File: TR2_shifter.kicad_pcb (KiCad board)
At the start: 2 copper layers, 69.2 x 29.8 mm, 28 parts, among them U1 LM339_DIP, U2 LM339_DIP

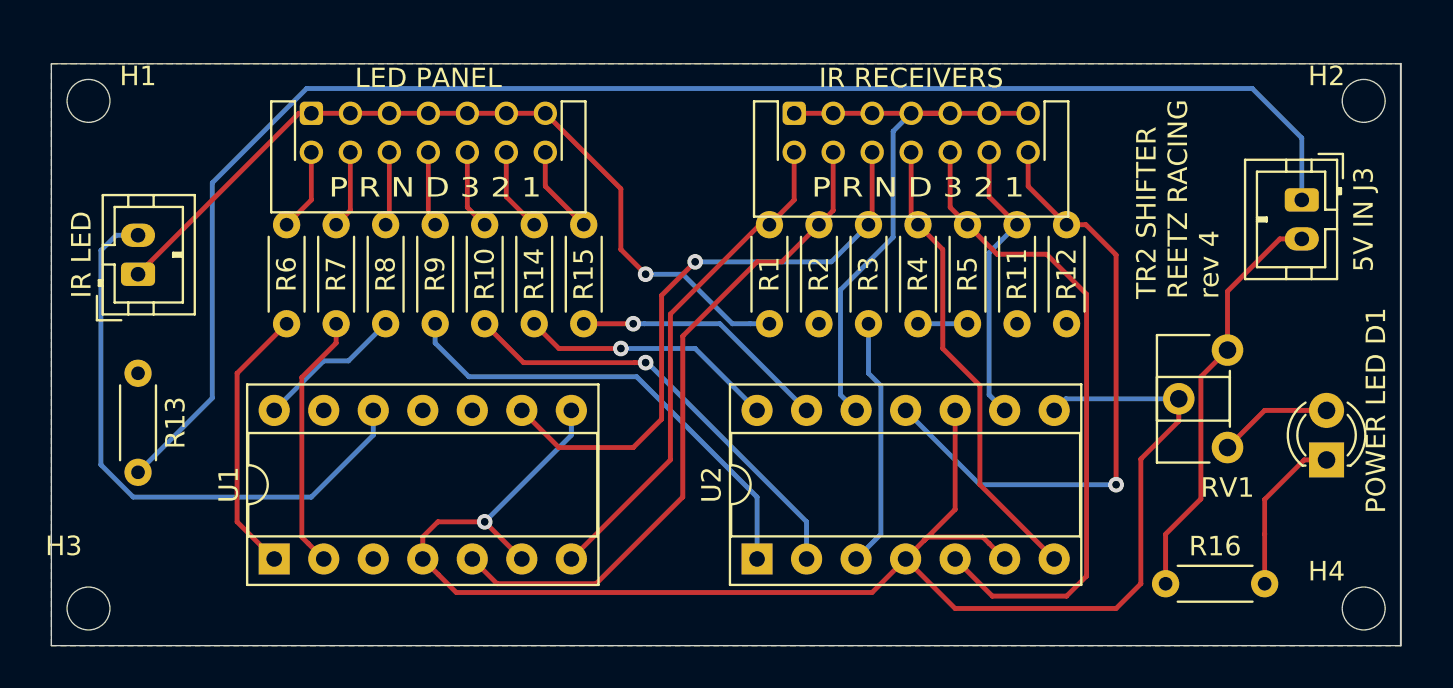
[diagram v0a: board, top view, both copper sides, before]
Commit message: Update silk and shift a few components
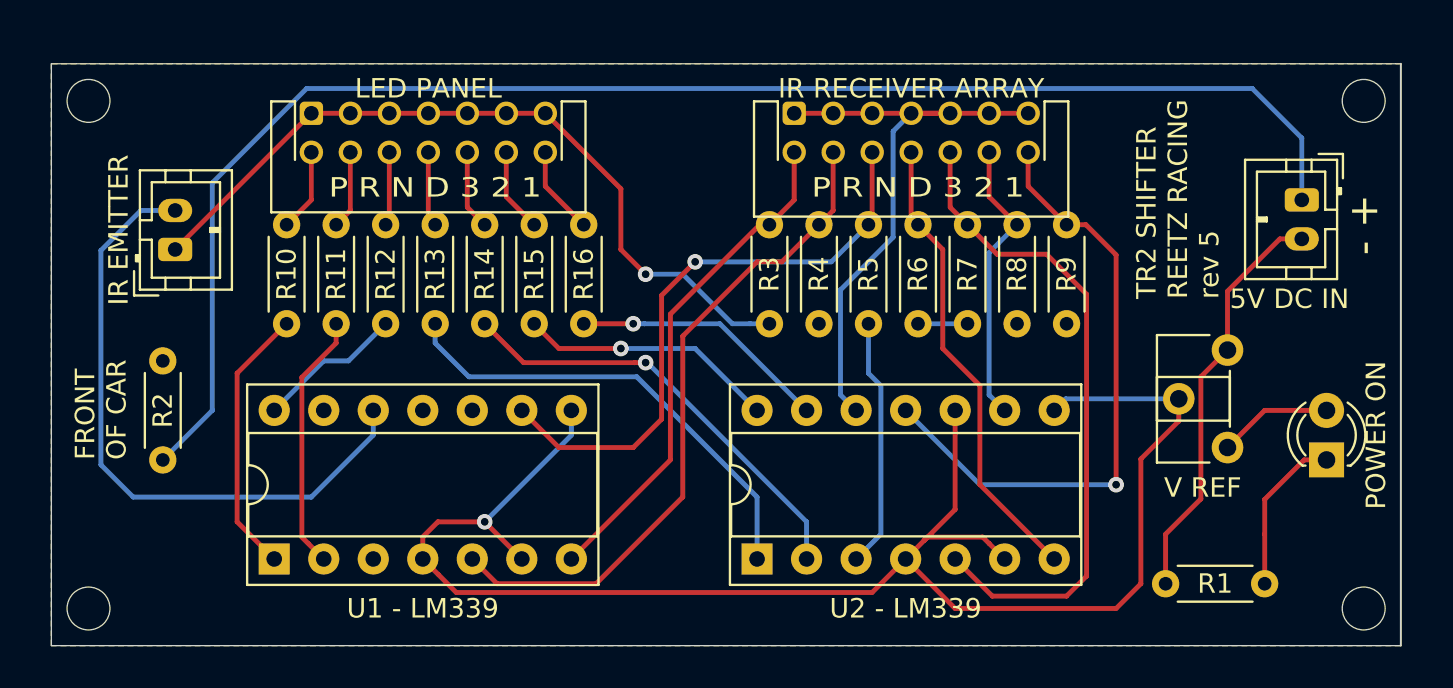
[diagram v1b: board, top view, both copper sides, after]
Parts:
- 5V DC IN: renamed from 5V IN J3
- IR EMITTER: renamed from IR LED
- IR RECEIVER ARRAY: renamed from IR RECEIVERS
- POWER ON: renamed from POWER LED D1
- U1 - LM339: renamed from U1
- U2 - LM339: renamed from U2
- V REF: renamed from RV1
- moved IR EMITTER 2.29 mm to (158.1, 78.1)
- moved R2 1.42 mm to (157.5, 83.8)
- renumbered R16 to R1, R6 to R10, R7 to R11, R8 to R12, R9 to R13, R10 to R14, R14 to R15, R15 to R16, R13 to R2, R1 to R3, R2 to R4, R3 to R5, R4 to R6, R5 to R7, R11 to R8, R12 to R9
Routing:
- net GND: track 82.8 -> 85.2 mm
- net +5V: track 63.4 -> 60.9 mm
- net Net-(J3-Pad1): track 78.5 -> 77.4 mm
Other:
- board text added: "+ -"
- board text added: "FRONT OF CAR"
- board text added: "TR2 SHIFTER REETZ RACING rev 5"
- board text removed: "TR2 SHIFTER REETZ RACING rev 4"

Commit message: Fix ground / power plane association with power pins
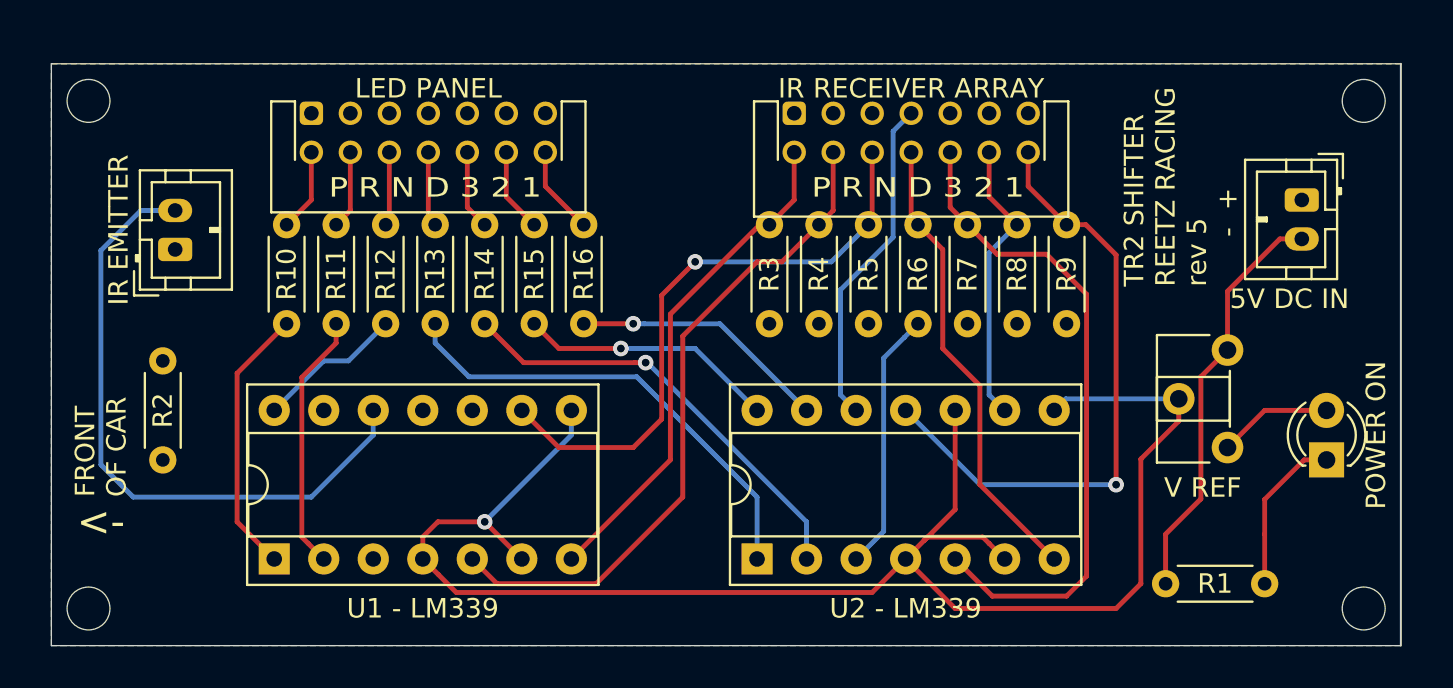
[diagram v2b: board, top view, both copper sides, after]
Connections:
- 5V DC IN pad 1: Net-(J3-Pad1) -> +5V
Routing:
- net Net-(J3-Pad1): track 77.4 -> 0.00 mm
- net +5V: track 60.9 -> 19.2 mm, vias 1 -> 0
- net GND: track 85.2 -> 71.2 mm
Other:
- board text added: "->"
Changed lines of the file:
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@@
   (general
     (thickness 1.6)
-    (drawings 9)
-    (tracks 177)
+    (drawings 10)
+    (tracks 158)
     (zones 0)
     (modules 28)
@@
     (mod_text_size 1 1)
     (mod_text_width 0.15)
-    (pad_size 1.524 1.524)
-    (pad_drill 0.762)
+    (pad_size 1.2 1.75)
+    (pad_drill 0.75)
     (pad_to_mask_clearance 0.051)
     (solder_mask_min_width 0.25)
@@
     (pad 2 thru_hole oval (at 2 0 270) (size 1.2 1.75) (drill 0.75) (layers *.Cu *.Mask)
       (net 1 GND))
-    (pad 1 thru_hole roundrect (at 0 0 270) (size 1.2 1.75) (drill 0.75) (layers *.Cu *.Mask) (roundrect_rratio 0.208333)
-      (net 20 "Net-(J3-Pad1)"))
+    (pad 1 thru_hole roundrect (at 0 0 270) (size 1.2 1.75) (drill 0.75) (layers *.Cu *.Mask) (roundrect_rratio 0.208)
+      (net 7 +5V))
     (model ${KISYS3DMOD}/Connector_JST.3dshapes/JST_PH_B2B-PH-K_1x02_P2.00mm_Vertical.wrl
       (at (xyz 0 0 0))
@@
     )
   )
-  (gr_text "+ -" (at 219.075 76.835 90) (layer F.SilkS)
+  (gr_text -> (at 154.305 92.075) (layer F.SilkS)
     (effects (font (size 1.5 1.5) (thickness 0.3)) (justify mirror))
   )
-  (gr_text "FRONT \nOF CAR" (at 154.305 88.9 90) (layer F.SilkS)
+  (gr_text "+  -" (at 212.09 76.2 90) (layer F.SilkS)
+    (effects (font (size 1 1) (thickness 0.25)) (justify mirror))
+  )
+  (gr_text "FRONT \nOF CAR" (at 154.305 90.805 90) (layer F.SilkS)
     (effects (font (size 1 1) (thickness 0.25)) (justify left))
   )
@@
     (effects (font (size 1 1.2) (thickness 0.15)))
   )
-  (gr_text "TR2 SHIFTER\nREETZ RACING\nrev 5" (at 209.55 80.645 90) (layer F.SilkS)
+  (gr_text "TR2 SHIFTER\nREETZ RACING\nrev 5" (at 208.915 80.01 90) (layer F.SilkS)
     (effects (font (size 1 1) (thickness 0.25)) (justify left))
   )
@@
   (segment (start 168.275 87.63) (end 168.275 86.36) (width 0.25) (layer B.Cu) (net 1))
   (segment (start 165.1 90.805) (end 168.275 87.63) (width 0.25) (layer B.Cu) (net 1))
-  (segment (start 201.865 71.12) (end 189.865 71.12) (width 0.25) (layer F.Cu) (net 1))
-  (segment (start 195.865 71.12) (end 197.865 71.12) (width 0.25) (layer F.Cu) (net 1))
   (segment (start 194.939999 72.045001) (end 194.939999 77.475001) (width 0.25) (layer B.Cu) (net 1))
   (segment (start 195.865 71.12) (end 194.939999 72.045001) (width 0.25) (layer B.Cu) (net 1))
@@
   (segment (start 203.835 95.885) (end 200.025 95.885) (width 0.25) (layer F.Cu) (net 6))
   (segment (start 200.025 95.885) (end 198.12 93.98) (width 0.25) (layer F.Cu) (net 6))
-  (segment (start 177.1 71.12) (end 165.1 71.12) (width 0.25) (layer F.Cu) (net 7))
-  (segment (start 193.675 81.915) (end 193.675 84.455) (width 0.25) (layer B.Cu) (net 7))
-  (segment (start 193.675 84.455) (end 194.31 85.09) (width 0.25) (layer B.Cu) (net 7))
   (segment (start 213.995 86.36) (end 212.09 88.265) (width 0.25) (layer F.Cu) (net 7))
   (segment (start 217.17 86.36) (end 213.995 86.36) (width 0.25) (layer F.Cu) (net 7))
-  (segment (start 177.1 71.12) (end 180.975 74.995) (width 0.25) (layer F.Cu) (net 7))
-  (segment (start 180.975 74.995) (end 180.975 78.105) (width 0.25) (layer F.Cu) (net 7))
-  (segment (start 180.975 78.105) (end 182.245 79.375) (width 0.25) (layer F.Cu) (net 7))
-  (via (at 182.245 79.375) (size 0.8) (drill 0.4) (layers F.Cu B.Cu) (net 7))
-  (segment (start 196.215 81.915) (end 198.755 81.915) (width 0.25) (layer B.Cu) (net 7))
-  (segment (start 194.31 92.71) (end 193.04 93.98) (width 0.25) (layer B.Cu) (net 7))
-  (segment (start 194.31 85.09) (end 194.31 92.71) (width 0.25) (layer B.Cu) (net 7))
-  (segment (start 182.245 79.375) (end 184.15141 79.375) (width 0.25) (layer B.Cu) (net 7))
-  (segment (start 187.605051 81.915) (end 188.595 81.915) (width 0.25) (layer B.Cu) (net 7))
-  (segment (start 184.15141 79.375) (end 186.69141 81.915) (width 0.25) (layer B.Cu) (net 7))
-  (segment (start 186.69141 81.915) (end 187.605051 81.915) (width 0.25) (layer B.Cu) (net 7))
-  (segment (start 165.1 71.12) (end 158.115 78.105) (width 0.25) (layer F.Cu) (net 7))
+  (segment (start 195.515001 82.614999) (end 196.215 81.915) (width 0.25) (layer B.Cu) (net 7))
+  (segment (start 194.454999 83.675001) (end 195.515001 82.614999) (width 0.25) (layer B.Cu) (net 7))
+  (segment (start 194.454999 92.565001) (end 194.454999 83.675001) (width 0.25) (layer B.Cu) (net 7))
+  (segment (start 193.04 93.98) (end 194.454999 92.565001) (width 0.25) (layer B.Cu) (net 7))
   (segment (start 165.1 75.565) (end 163.83 76.835) (width 0.25) (layer F.Cu) (net 8))
   (segment (start 165.1 73.12) (end 165.1 75.565) (width 0.25) (layer F.Cu) (net 8))
@@
   (via (at 173.99 92.075) (size 0.8) (drill 0.4) (layers F.Cu B.Cu) (net 19))
   (segment (start 178.435 87.63) (end 173.99 92.075) (width 0.25) (layer B.Cu) (net 19))
-  (segment (start 160.02 74.68681) (end 160.02 86.36) (width 0.25) (layer B.Cu) (net 20))
-  (segment (start 160.02 86.36) (end 157.48 88.9) (width 0.25) (layer B.Cu) (net 20))
-  (segment (start 164.85681 69.85) (end 160.02 74.68681) (width 0.25) (layer B.Cu) (net 20))
-  (segment (start 215.9 72.39) (end 213.36 69.85) (width 0.25) (layer B.Cu) (net 20))
-  (segment (start 213.36 69.85) (end 164.85681 69.85) (width 0.25) (layer B.Cu) (net 20))
-  (segment (start 215.9 75.565) (end 215.9 72.39) (width 0.25) (layer B.Cu) (net 20))
   (segment (start 213.995 92.71) (end 213.995 95.25) (width 0.25) (layer F.Cu) (net 21))
   (segment (start 213.995 90.925) (end 213.995 92.71) (width 0.25) (layer F.Cu) (net 21))

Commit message: Make board 30x70mm, offset hole centers from board edge by 2mm
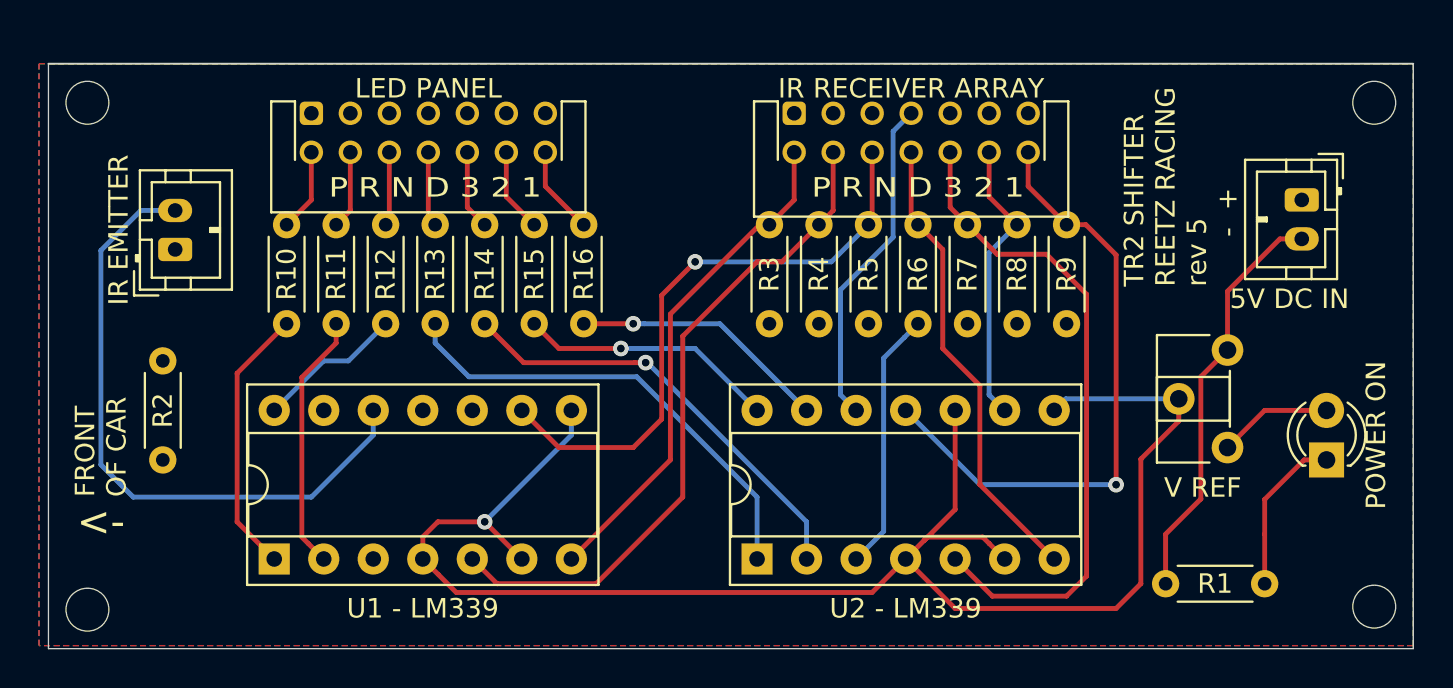
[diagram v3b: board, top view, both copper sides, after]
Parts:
- moved H2 0.55 mm to (219.6, 70.6)
- moved H4 0.55 mm to (219.6, 96.4)
- moved H1 0.11 mm to (153.6, 70.6)
- moved H3 0.08 mm to (153.6, 96.6)
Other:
- board size 69.2 x 29.8 mm -> 70 x 30 mm
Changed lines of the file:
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@@
   )
   (module MountingHole:MountingHole_2.2mm_M2 (layer F.Cu)
-    (at 219.075 96.52)
+    (at 219.615 96.425)
     (descr "Mounting Hole 2.2mm, no annular, M2")
     (tags "mounting hole 2.2mm no annular m2")
@@
   )
   (module MountingHole:MountingHole_2.2mm_M2 (layer F.Cu)
-    (at 153.67 96.52)
+    (at 153.615 96.58)
     (descr "Mounting Hole 2.2mm, no annular, M2")
     (tags "mounting hole 2.2mm no annular m2")
@@
   )
   (module MountingHole:MountingHole_2.2mm_M2 (layer F.Cu)
-    (at 219.075 70.485)
+    (at 219.615 70.58)
     (descr "Mounting Hole 2.2mm, no annular, M2")
     (tags "mounting hole 2.2mm no annular m2")
@@
   )
   (module MountingHole:MountingHole_2.2mm_M2 (layer F.Cu)
-    (at 153.67 70.485)
+    (at 153.615 70.58)
     (descr "Mounting Hole 2.2mm, no annular, M2")
     (tags "mounting hole 2.2mm no annular m2")
@@
     )
   )
+  (gr_line (start 221.615 98.58) (end 221.615 68.58) (layer Edge.Cuts) (width 0.05))
+  (gr_line (start 151.615 98.58) (end 221.615 98.58) (layer Edge.Cuts) (width 0.05))
+  (gr_line (start 151.615 68.58) (end 151.615 98.58) (layer Edge.Cuts) (width 0.05))
+  (gr_line (start 151.615 68.58) (end 221.615 68.58) (layer Edge.Cuts) (width 0.1))
   (gr_text -> (at 154.305 92.075) (layer F.SilkS)
     (effects (font (size 1.5 1.5) (thickness 0.3)) (justify mirror))
@@
     (effects (font (size 1 1) (thickness 0.25)) (justify left))
   )
-  (gr_line (start 220.98 68.58) (end 151.765 68.58) (layer Edge.Cuts) (width 0.05))
-  (gr_line (start 151.765 98.425) (end 151.765 68.58) (layer Edge.Cuts) (width 0.05))
-  (gr_line (start 220.98 98.425) (end 151.765 98.425) (layer Edge.Cuts) (width 0.05))
   (gr_text "P R N D 3 2 1" (at 196.215 74.93) (layer F.SilkS)
     (effects (font (size 1 1.2) (thickness 0.15)))
@@
     (effects (font (size 1 1) (thickness 0.25)) (justify left))
   )
-  (gr_line (start 220.98 68.58) (end 220.98 98.425) (layer Edge.Cuts) (width 0.1))
   (segment (start 214.775 77.565) (end 215.9 77.565) (width 0.25) (layer F.Cu) (net 1))
   (segment (start 212.09 80.25) (end 214.775 77.565) (width 0.25) (layer F.Cu) (net 1))
@@
   (segment (start 177.1 74.865) (end 179.07 76.835) (width 0.25) (layer F.Cu) (net 16))
   (segment (start 177.1 73.12) (end 177.1 74.865) (width 0.25) (layer F.Cu) (net 16))
-  (segment (start 168.91 81.915) (end 167.005 83.82) (width 0.25) (layer B.Cu) (net 25))
-  (segment (start 165.735 83.82) (end 163.195 86.36) (width 0.25) (layer B.Cu) (net 25))
-  (segment (start 167.005 83.82) (end 165.735 83.82) (width 0.25) (layer B.Cu) (net 25))
-  (segment (start 173.180052 84.635001) (end 181.790001 84.635001) (width 0.25) (layer B.Cu) (net 26))
-  (segment (start 181.790001 84.635001) (end 187.96 90.805) (width 0.25) (layer B.Cu) (net 26))
-  (segment (start 171.45 82.904949) (end 173.180052 84.635001) (width 0.25) (layer B.Cu) (net 26))
-  (segment (start 187.96 90.805) (end 187.96 93.98) (width 0.25) (layer B.Cu) (net 26))
-  (segment (start 171.45 81.915) (end 171.45 82.904949) (width 0.25) (layer B.Cu) (net 26))
   (segment (start 173.99 81.915) (end 175.985001 83.910001) (width 0.25) (layer F.Cu) (net 17))
   (segment (start 190.5 92.075) (end 182.245 83.82) (width 0.25) (layer B.Cu) (net 17))
@@
   (segment (start 184.785 83.185) (end 187.96 86.36) (width 0.25) (layer B.Cu) (net 18))
   (segment (start 180.975 83.185) (end 184.785 83.185) (width 0.25) (layer B.Cu) (net 18))
-  (segment (start 179.07 81.915) (end 181.609996 81.915) (width 0.25) (layer F.Cu) (net 27))
-  (via (at 181.609996 81.915) (size 0.8) (drill 0.4) (layers F.Cu B.Cu) (net 27))
-  (segment (start 182.175681 81.915) (end 181.609996 81.915) (width 0.25) (layer B.Cu) (net 27))
-  (segment (start 190.5 86.36) (end 186.055 81.915) (width 0.25) (layer B.Cu) (net 27))
-  (segment (start 186.055 81.915) (end 182.175681 81.915) (width 0.25) (layer B.Cu) (net 27))
   (segment (start 207.645 88.855512) (end 207.645 95.25) (width 0.25) (layer F.Cu) (net 19))
   (segment (start 209.59 86.910512) (end 207.645 88.855512) (width 0.25) (layer F.Cu) (net 19))
@@
   (segment (start 166.37 82.904949) (end 164.609999 84.66495) (width 0.25) (layer F.Cu) (net 24))
   (segment (start 166.37 81.915) (end 166.37 82.904949) (width 0.25) (layer F.Cu) (net 24))
+  (segment (start 168.91 81.915) (end 167.005 83.82) (width 0.25) (layer B.Cu) (net 25))
+  (segment (start 165.735 83.82) (end 163.195 86.36) (width 0.25) (layer B.Cu) (net 25))
+  (segment (start 167.005 83.82) (end 165.735 83.82) (width 0.25) (layer B.Cu) (net 25))
+  (segment (start 173.180052 84.635001) (end 181.790001 84.635001) (width 0.25) (layer B.Cu) (net 26))
+  (segment (start 181.790001 84.635001) (end 187.96 90.805) (width 0.25) (layer B.Cu) (net 26))
+  (segment (start 171.45 82.904949) (end 173.180052 84.635001) (width 0.25) (layer B.Cu) (net 26))
+  (segment (start 187.96 90.805) (end 187.96 93.98) (width 0.25) (layer B.Cu) (net 26))
+  (segment (start 171.45 81.915) (end 171.45 82.904949) (width 0.25) (layer B.Cu) (net 26))
+  (segment (start 179.07 81.915) (end 181.609996 81.915) (width 0.25) (layer F.Cu) (net 27))
+  (via (at 181.609996 81.915) (size 0.8) (drill 0.4) (layers F.Cu B.Cu) (net 27))
+  (segment (start 182.175681 81.915) (end 181.609996 81.915) (width 0.25) (layer B.Cu) (net 27))
+  (segment (start 190.5 86.36) (end 186.055 81.915) (width 0.25) (layer B.Cu) (net 27))
+  (segment (start 186.055 81.915) (end 182.175681 81.915) (width 0.25) (layer B.Cu) (net 27))
   (zone (net 7) (net_name +5V) (layer B.Cu) (hatch edge 0.508)
     (connect_pads (clearance 0.508))
@@
     (polygon
       (pts
-        (xy 220.98 98.425) (xy 151.765 98.425) (xy 151.765 68.58) (xy 220.98 68.58)
+        (xy 221.615 98.425) (xy 151.13 98.425) (xy 151.13 68.58) (xy 221.615 68.58)
       )
     )
@@
     (polygon
       (pts
-        (xy 220.98 98.425) (xy 151.765 98.425) (xy 151.765 68.58) (xy 220.98 68.58)
+        (xy 221.615 98.425) (xy 151.13 98.425) (xy 151.13 68.58) (xy 221.615 68.58)
       )
     )

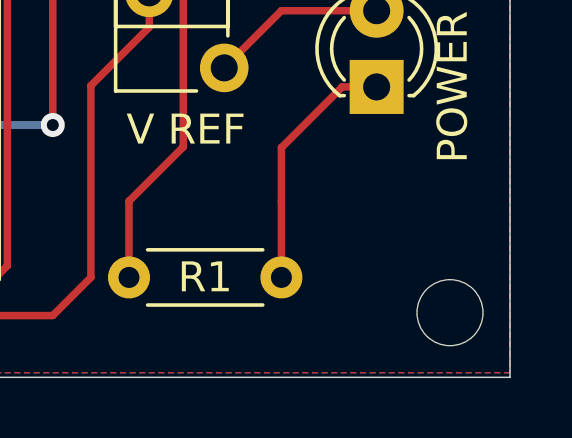
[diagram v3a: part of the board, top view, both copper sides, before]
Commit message: Adjust one mounting hole that had wrong Y dimension
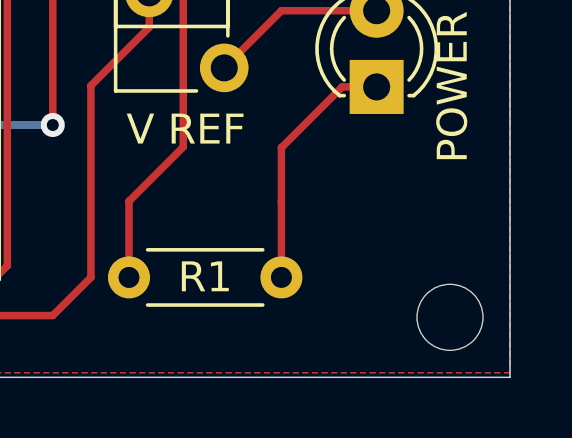
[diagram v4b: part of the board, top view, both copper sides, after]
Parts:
- moved H4 0.16 mm to (219.6, 96.6)
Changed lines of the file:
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@@
   )
   (module MountingHole:MountingHole_2.2mm_M2 (layer F.Cu)
-    (at 219.615 96.425)
+    (at 219.615 96.58)
     (descr "Mounting Hole 2.2mm, no annular, M2")
     (tags "mounting hole 2.2mm no annular m2")
